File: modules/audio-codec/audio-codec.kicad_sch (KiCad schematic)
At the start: 24 parts, among them U1 TLV320AIC3110IRHBR, U2 ADP5301ACBZ-1-R7

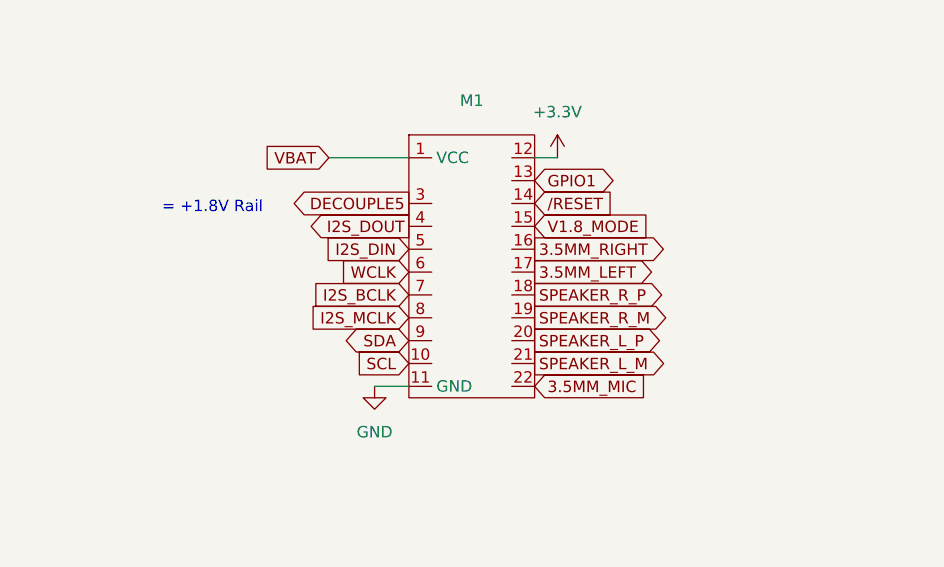
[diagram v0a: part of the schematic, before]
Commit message: outstanding changes to audio codec module
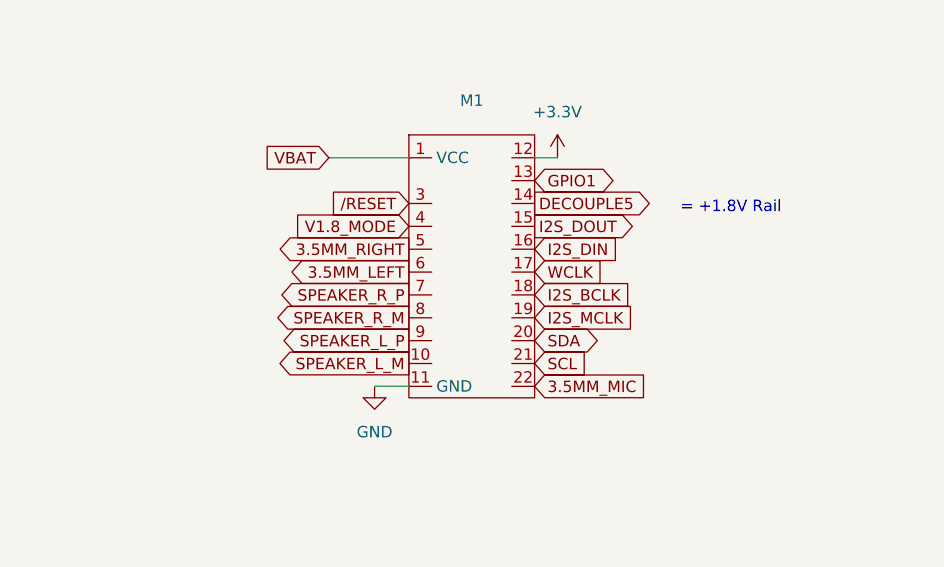
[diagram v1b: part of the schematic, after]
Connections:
- net 3.5MM_LEFT: now also M1.6; no longer M1.17
- net 3.5MM_RIGHT: now also M1.5; no longer M1.16
- net DECOUPLE5: now also M1.14; no longer M1.3
- net I2S_BCLK: now also M1.18; no longer M1.7
- net I2S_DIN: now also M1.16; no longer M1.5
- net I2S_DOUT: now also M1.15; no longer M1.4
- net I2S_MCLK: now also M1.19; no longer M1.8
- net SCL: now also M1.21; no longer M1.10
- net SDA: now also M1.20; no longer M1.9
- net SPEAKER_L_M: now also M1.10; no longer M1.21
- net SPEAKER_L_P: now also M1.9; no longer M1.20
- net SPEAKER_R_M: now also M1.8; no longer M1.19
- net SPEAKER_R_P: now also M1.7; no longer M1.18
- net V1.8_MODE: now also M1.4; no longer M1.15
- net WCLK: now also M1.17; no longer M1.6
- net /RESET: now also M1.3; no longer M1.14

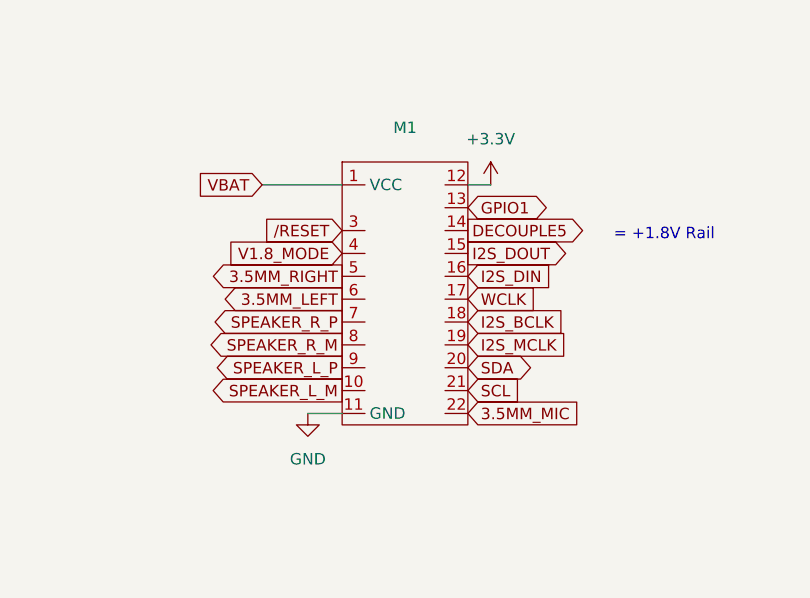
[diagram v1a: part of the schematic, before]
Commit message: update audio codec module footprint and generate gerbers
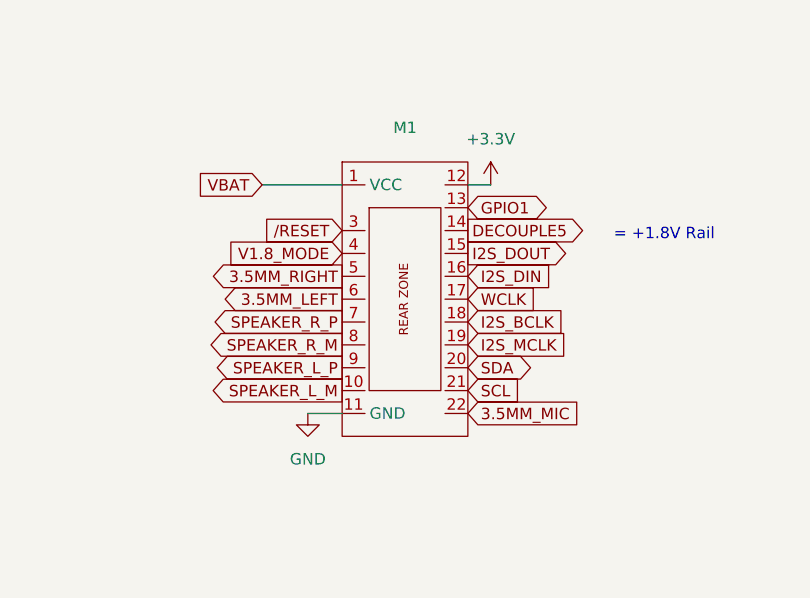
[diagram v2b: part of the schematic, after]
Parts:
- removed M1: ~, MegaCastle:MegaCastle2x11Wide-Module-I13.2x22.25, symbol MegaCastle:MegaCastle2x11-Module
- added M1: ~, MegaCastle:MegaCastle2x11-Module-I17.7x23.1-MBFFFFC-PANEL-NIBBLE, symbol MegaCastle:MegaCastle2x11-Module-I17.7x23.1-MBFFFFC
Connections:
- net +3.3V: now also M1.12
- net 3.5MM_LEFT: now also M1.6
- net 3.5MM_MIC: now also M1.22
- net 3.5MM_RIGHT: now also M1.5
- net DECOUPLE1: now also M1.1 (VCC)
- net DECOUPLE5: now also M1.14
- net GND: now also M1.11 (GND)
- net GPIO1: now also M1.13
- net I2S_BCLK: now also M1.18
- net I2S_DIN: now also M1.16
- net I2S_DOUT: now also M1.15
- net I2S_MCLK: now also M1.19
- net SCL: now also M1.21
- net SDA: now also M1.20
- net SPEAKER_L_M: now also M1.10
- net SPEAKER_L_P: now also M1.9
- net SPEAKER_R_M: now also M1.8
- net SPEAKER_R_P: now also M1.7
- net V1.8_MODE: now also M1.4
- net WCLK: now also M1.17
- net /RESET: now also M1.3
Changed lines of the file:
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@@
+	)
+	(symbol
+		(lib_id "MegaCastle:MegaCastle2x11-Module-I17.7x23.1-MBFFFFC")
+		(at 100.33 125.73 0)
+		(unit 1)
+		(exclude_from_sim no)
+		(in_bom yes)
+		(on_board yes)
+		(dnp no)
+		(fields_autoplaced yes)
+		(property "Reference" "M1"
+			(at 100.965 106.68 0)
+			(effects
+				(font
+					(size 1.27 1.27)
+				)
+			)
+		)
+		(property "Value" "~"
+			(at 100.965 109.22 0)
+			(effects
+				(font
+					(size 1.27 1.27)
+				)
+			)
+		)
+		(property "Footprint" "MegaCastle:MegaCastle2x11-Module-I17.7x23.1-MBFFFFC-PANEL-NIBBLE"
+			(at 100.33 146.05 0)
+			(effects
+				(font
+					(size 1.27 1.27)
+				)
+				(hide yes)
+			)
+		)
+		(property "Datasheet" ""
+			(at 100.33 120.65 0)
+			(effects
+				(font
+					(size 1.27 1.27)
+				)
+				(hide yes)
+			)
+		)
+		(property "Description" "Generated using footprint-gen .. 17.7 22.25 21 1"
+			(at 100.33 125.73 0)
+			(effects
+				(font
+					(size 1.27 1.27)
+				)
+				(hide yes)
+			)
+		)
+		(pin "8"
+		)
+		(pin "13"
+		)
+		(pin "11"
+		)
+		(pin "12"
+		)
+		(pin "1"
+		)
+		(pin "10"
+		)
+		(pin "5"
+		)
+		(pin "6"
+		)
+		(pin "15"
+		)
+		(pin "4"
+		)
+		(pin "22"
+		)
+		(pin "3"
+		)
+		(pin "18"
+		)
+		(pin "17"
+		)
+		(pin "14"
+		)
+		(pin "21"
+		)
+		(pin "20"
+		)
+		(pin "9"
+		)
+		(pin "16"
+		)
+		(pin "7"
+		)
+		(pin "19"
+		)
+		(instances
+			(project ""
+				(path "/e0031877-65b0-4e57-86fe-bc20869de862"
+					(reference "M1")
+					(unit 1)
+				)
+			)
+		)
 	)
 	(symbol
@@
 					(unit 1)
 				)
-			)
-		)
-	)
-	(symbol
-		(lib_id "MegaCastle:MegaCastle2x11-Module")
-		(at 100.33 124.46 0)
-		(unit 1)
-		(exclude_from_sim no)
-		(in_bom yes)
-		(on_board yes)
-		(dnp no)
-		(fields_autoplaced yes)
-		(property "Reference" "M1"
-			(at 100.965 106.68 0)
-			(effects
-				(font
-					(size 1.27 1.27)
-				)
-			)
-		)
-		(property "Value" "~"
-			(at 100.965 109.22 0)
-			(effects
-				(font
-					(size 1.27 1.27)
-				)
-			)
-		)
-		(property "Footprint" "MegaCastle:MegaCastle2x11Wide-Module-I13.2x22.25"
-			(at 100.33 119.38 0)
-			(effects
-				(font
-					(size 1.27 1.27)
-				)
-				(hide yes)
-			)
-		)
-		(property "Datasheet" ""
-			(at 100.33 119.38 0)
-			(effects
-				(font
-					(size 1.27 1.27)
-				)
-				(hide yes)
-			)
-		)
-		(property "Description" ""
-			(at 100.33 124.46 0)
-			(effects
-				(font
-					(size 1.27 1.27)
-				)
-				(hide yes)
-			)
-		)
-		(pin "3"
-		)
-		(pin "18"
-		)
-		(pin "8"
-		)
-		(pin "6"
-		)
-		(pin "9"
-		)
-		(pin "21"
-		)
-		(pin "4"
-		)
-		(pin "20"
-		)
-		(pin "11"
-		)
-		(pin "1"
-		)
-		(pin "10"
-		)
-		(pin "17"
-		)
-		(pin "16"
-		)
-		(pin "5"
-		)
-		(pin "14"
-		)
-		(pin "15"
-		)
-		(pin "22"
-		)
-		(pin "7"
-		)
-		(pin "19"
-		)
-		(pin "12"
-		)
-		(pin "13"
-		)
-		(instances
-			(project ""
-				(path "/e0031877-65b0-4e57-86fe-bc20869de862"
-					(reference "M1")
-					(unit 1)
-				)
